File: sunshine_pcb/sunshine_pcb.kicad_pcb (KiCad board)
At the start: 4 copper layers, 45.5 x 66.7 mm, 54 parts, among them J1 PWRIN, J2 Conn_01x04, J3 PWROUT, J5 VerticalUSB, Q1 AO3400A, SW1 SW_SPST, U1 ESP32-S3-WROOM-1, U2 SPX1117M3, U3 LIS3MDL, U4 ADXL375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

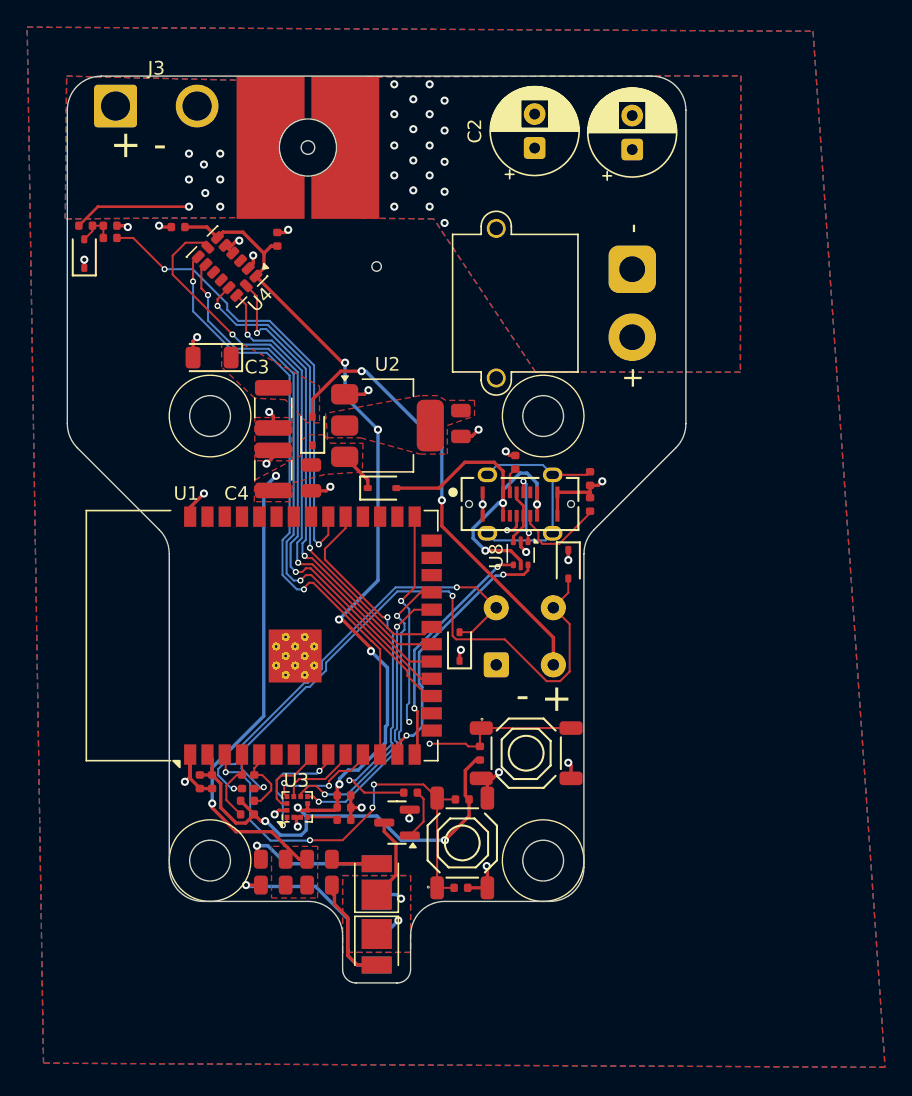
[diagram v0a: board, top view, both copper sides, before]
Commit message: Fix VSENSE net
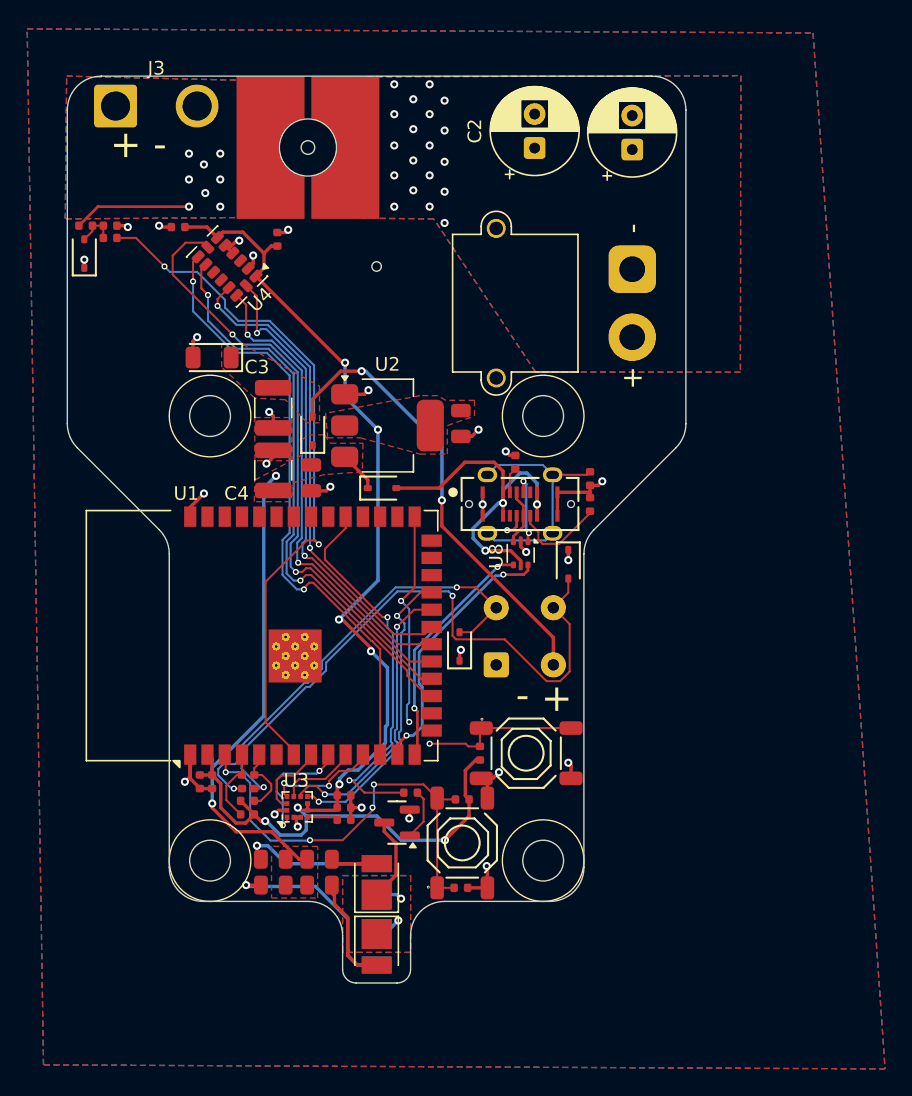
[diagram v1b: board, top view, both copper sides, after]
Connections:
- U1 pad 32: /VSENSE -> unconnected-(U1-IO39-Pad32)
- U1 pad 7: unconnected-(U1-IO7-Pad7) -> /VSENSE
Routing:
- net /VSENSE: track 34.3 -> 50.9 mm
